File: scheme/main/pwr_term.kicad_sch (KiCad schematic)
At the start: 1 part, among them J1 DG45C-B-06P-13-00A

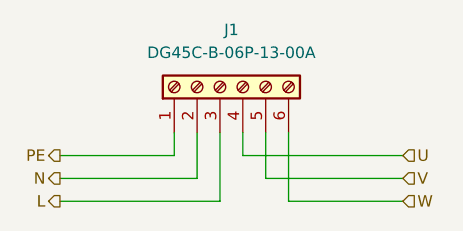
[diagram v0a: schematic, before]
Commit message: toplevel layout, can bus
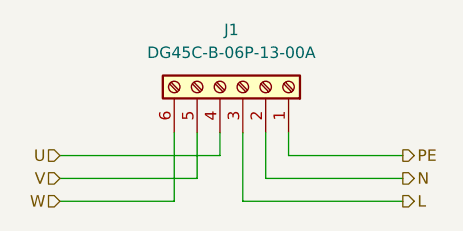
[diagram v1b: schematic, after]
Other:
- moved on the sheet: J1
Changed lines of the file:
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@@
 	(wire
 		(pts
-			(xy 138.43 97.79) (xy 151.13 97.79)
-		)
-		(stroke
-			(width 0)
-			(type default)
-		)
-	)
-	(wire
-		(pts
-			(xy 156.21 102.87) (xy 156.21 95.25)
-		)
-		(stroke
-			(width 0)
-			(type default)
-		)
-	)
-	(wire
-		(pts
-			(xy 176.53 97.79) (xy 158.75 97.79)
+			(xy 176.53 97.79) (xy 163.83 97.79)
+		)
+		(stroke
+			(width 0)
+			(type default)
+		)
+	)
+	(wire
+		(pts
+			(xy 158.75 102.87) (xy 158.75 95.25)
+		)
+		(stroke
+			(width 0)
+			(type default)
+		)
+	)
+	(wire
+		(pts
+			(xy 138.43 97.79) (xy 156.21 97.79)
+		)
+		(stroke
+			(width 0)
+			(type default)
+		)
+	)
+	(wire
+		(pts
+			(xy 153.67 100.33) (xy 153.67 95.25)
+		)
+		(stroke
+			(width 0)
+			(type default)
+		)
+	)
+	(wire
+		(pts
+			(xy 156.21 97.79) (xy 156.21 95.25)
+		)
+		(stroke
+			(width 0)
+			(type default)
+		)
+	)
+	(wire
+		(pts
+			(xy 176.53 100.33) (xy 161.29 100.33)
+		)
+		(stroke
+			(width 0)
+			(type default)
+		)
+	)
+	(wire
+		(pts
+			(xy 138.43 102.87) (xy 151.13 102.87)
+		)
+		(stroke
+			(width 0)
+			(type default)
+		)
+	)
+	(wire
+		(pts
+			(xy 138.43 100.33) (xy 153.67 100.33)
+		)
+		(stroke
+			(width 0)
+			(type default)
+		)
+	)
+	(wire
+		(pts
+			(xy 151.13 102.87) (xy 151.13 95.25)
+		)
+		(stroke
+			(width 0)
+			(type default)
+		)
+	)
+	(wire
+		(pts
+			(xy 163.83 97.79) (xy 163.83 95.25)
 		)
 		(stroke
@@
 	(wire
 		(pts
-			(xy 158.75 97.79) (xy 158.75 95.25)
-		)
-		(stroke
-			(width 0)
-			(type default)
-		)
-	)
-	(wire
-		(pts
-			(xy 138.43 100.33) (xy 153.67 100.33)
-		)
-		(stroke
-			(width 0)
-			(type default)
-		)
-	)
-	(wire
-		(pts
-			(xy 176.53 102.87) (xy 163.83 102.87)
-		)
-		(stroke
-			(width 0)
-			(type default)
-		)
-	)
-	(wire
-		(pts
-			(xy 176.53 100.33) (xy 161.29 100.33)
-		)
-		(stroke
-			(width 0)
-			(type default)
-		)
-	)
-	(wire
-		(pts
-			(xy 163.83 102.87) (xy 163.83 95.25)
-		)
-		(stroke
-			(width 0)
-			(type default)
-		)
-	)
-	(wire
-		(pts
-			(xy 151.13 97.79) (xy 151.13 95.25)
-		)
-		(stroke
-			(width 0)
-			(type default)
-		)
-	)
-	(wire
-		(pts
-			(xy 153.67 100.33) (xy 153.67 95.25)
-		)
-		(stroke
-			(width 0)
-			(type default)
-		)
-	)
-	(wire
-		(pts
-			(xy 138.43 102.87) (xy 156.21 102.87)
+			(xy 176.53 102.87) (xy 158.75 102.87)
 		)
 		(stroke
@@
 	(hierarchical_label "U"
 		(shape input)
-		(at 176.53 97.79 0)
-		(fields_autoplaced yes)
-		(effects
-			(font
-				(size 1.27 1.27)
-			)
-			(justify left)
+		(at 138.43 97.79 180)
+		(fields_autoplaced yes)
+		(effects
+			(font
+				(size 1.27 1.27)
+			)
+			(justify right)
 		)
 	)
 	(hierarchical_label "N"
 		(shape output)
-		(at 138.43 100.33 180)
-		(fields_autoplaced yes)
-		(effects
-			(font
-				(size 1.27 1.27)
-			)
-			(justify right)
+		(at 176.53 100.33 0)
+		(fields_autoplaced yes)
+		(effects
+			(font
+				(size 1.27 1.27)
+			)
+			(justify left)
 		)
 	)
 	(hierarchical_label "PE"
 		(shape output)
-		(at 138.43 97.79 180)
-		(fields_autoplaced yes)
-		(effects
-			(font
-				(size 1.27 1.27)
-			)
-			(justify right)
+		(at 176.53 97.79 0)
+		(fields_autoplaced yes)
+		(effects
+			(font
+				(size 1.27 1.27)
+			)
+			(justify left)
 		)
 	)
 	(hierarchical_label "L"
 		(shape output)
-		(at 138.43 102.87 180)
-		(fields_autoplaced yes)
-		(effects
-			(font
-				(size 1.27 1.27)
-			)
-			(justify right)
+		(at 176.53 102.87 0)
+		(fields_autoplaced yes)
+		(effects
+			(font
+				(size 1.27 1.27)
+			)
+			(justify left)
 		)
 	)
 	(hierarchical_label "W"
 		(shape input)
-		(at 176.53 102.87 0)
-		(fields_autoplaced yes)
-		(effects
-			(font
-				(size 1.27 1.27)
-			)
-			(justify left)
+		(at 138.43 102.87 180)
+		(fields_autoplaced yes)
+		(effects
+			(font
+				(size 1.27 1.27)
+			)
+			(justify right)
 		)
 	)
 	(hierarchical_label "V"
 		(shape input)
-		(at 176.53 100.33 0)
-		(fields_autoplaced yes)
-		(effects
-			(font
-				(size 1.27 1.27)
-			)
-			(justify left)
+		(at 138.43 100.33 180)
+		(fields_autoplaced yes)
+		(effects
+			(font
+				(size 1.27 1.27)
+			)
+			(justify right)
 		)
 	)
 	(symbol
 		(lib_id "Connector:Screw_Terminal_01x06")
-		(at 156.21 90.17 90)
+		(at 158.75 90.17 270)
+		(mirror x)
 		(unit 1)
 		(exclude_from_sim no)
@@
 		)
 		(property "Footprint" "main:DG45C-B-06P-13-00A"
-			(at 156.21 90.17 0)
+			(at 158.75 90.17 0)
 			(effects
 				(font
@@
 		)
 		(property "Datasheet" "https://www.platan.ru/cgi-bin/qwery.pl/id=2010007888"
-			(at 156.21 90.17 0)
+			(at 158.75 90.17 0)
 			(effects
 				(font
@@
 		)
 		(property "Description" "Generic screw terminal, single row, 01x06, script generated (kicad-library-utils/schlib/autogen/connector/)"
-			(at 156.21 90.17 0)
-			(effects
-				(font
+			(at 158.75 90.17 0)
+			(effects
+				(font
